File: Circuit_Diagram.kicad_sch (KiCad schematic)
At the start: 21 parts, among them IC1 HCPL-3120, Q2 Q_NMOS_GDS, U3 ACPL-C870, U4 ACS712xLCTR-30A

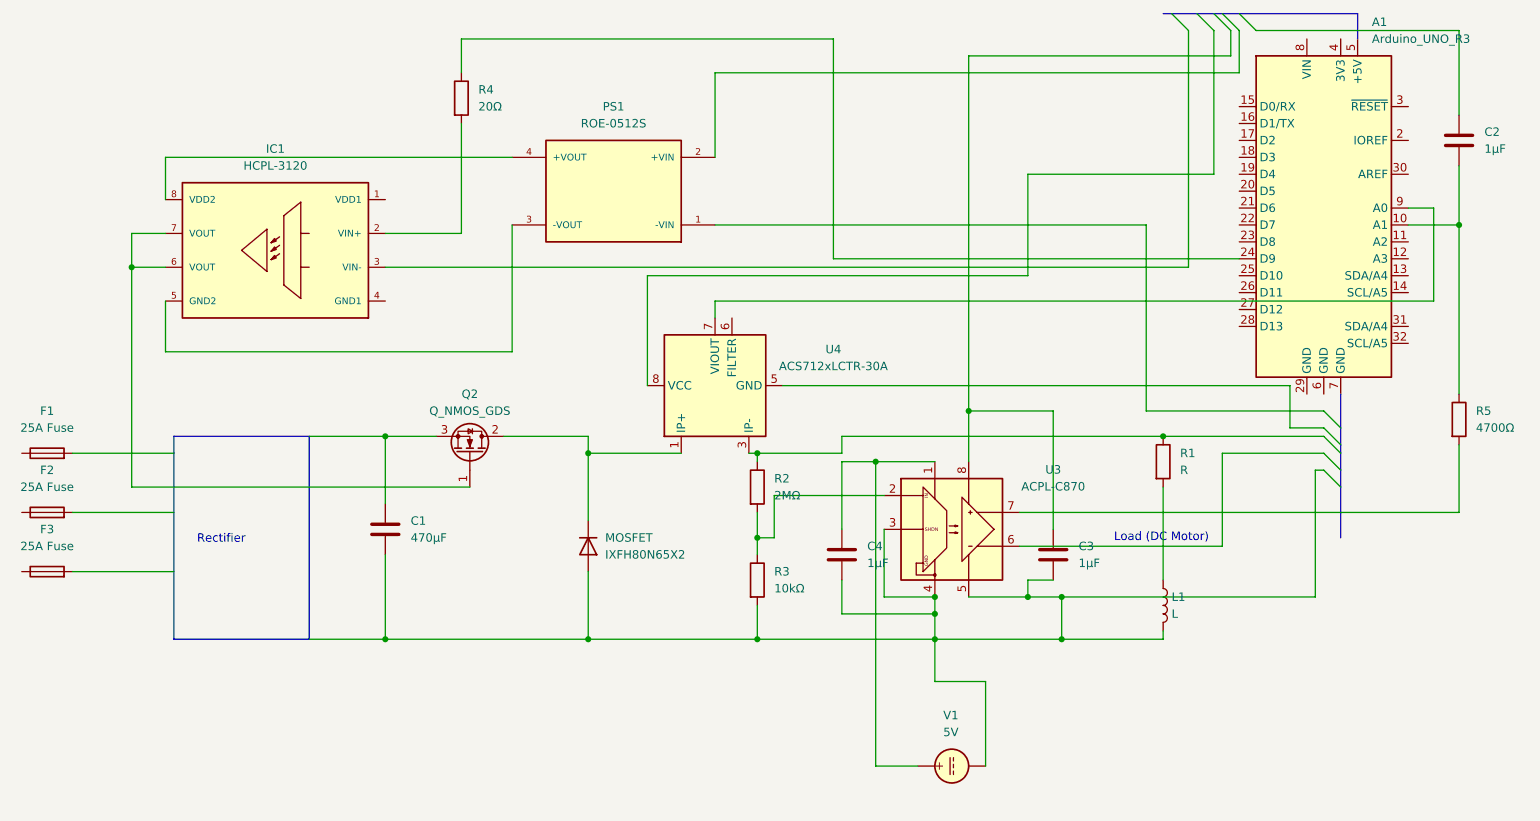
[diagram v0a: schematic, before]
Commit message: Updated wiring diagram
Added RC filter to voltage sensor output
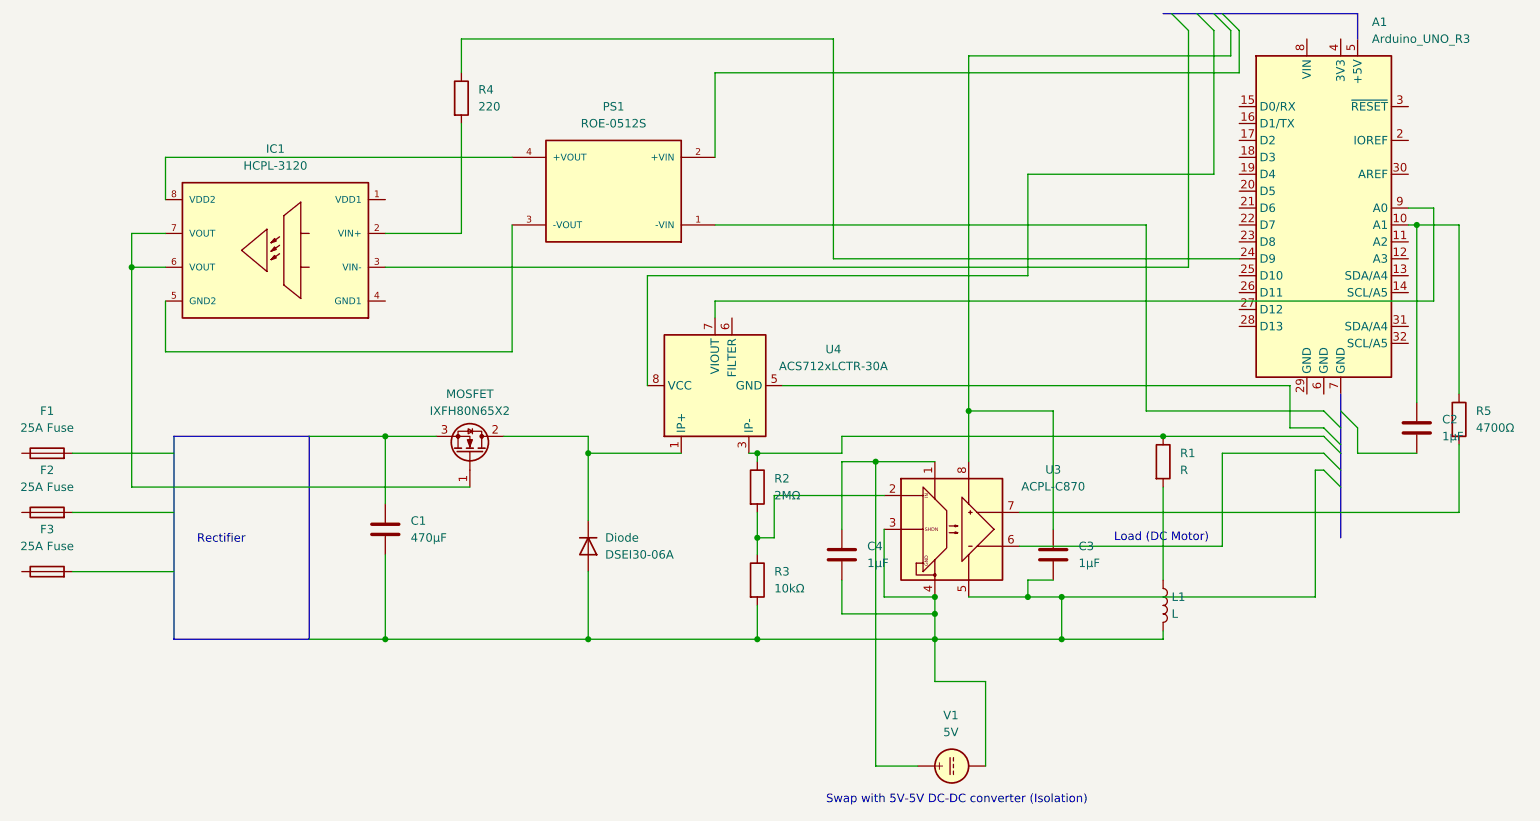
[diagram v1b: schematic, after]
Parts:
- Diode: renamed from MOSFET; value IXFH80N65X2 -> DSEI30-06A
- MOSFET: renamed from Q2; value Q_NMOS_GDS -> IXFH80N65X2
- R4: value 20Ω -> 220
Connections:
- net at A1.10 (A1), R5.1: now also C2.1; no longer C2.2
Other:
- note added: "Swap with 5V-5V DC-DC converter (Isolation)"
- moved on the sheet: C2
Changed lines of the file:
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@@
+		)
+	)
+	(text "Swap with 5V-5V DC-DC converter (Isolation)\n"
+		(exclude_from_sim no)
+		(at 158.242 132.08 0)
+		(effects
+			(font
+				(size 1.27 1.27)
+			)
 		)
 	)
@@
 	)
 	(junction
+		(at 227.33 45.72)
+		(diameter 0)
+		(color 0 0 0 0)
+	)
+	(junction
 		(at 72.39 77.47)
 		(diameter 0)
@@
 	)
 	(junction
-		(at 233.68 45.72)
-		(diameter 0)
-		(color 0 0 0 0)
-	)
-	(junction
 		(at 128.27 92.71)
 		(diameter 0)
@@
 	)
 	(bus_entry
-		(at 200.66 13.97)
-		(size 2.54 2.54)
-		(stroke
-			(width 0)
-			(type default)
-		)
-	)
-	(bus_entry
 		(at 213.36 76.2)
 		(size 2.54 2.54)
@@
 	)
 	(bus_entry
+		(at 215.9 73.66)
+		(size 2.54 2.54)
+		(stroke
+			(width 0)
+			(type default)
+		)
+	)
+	(bus_entry
 		(at 198.12 13.97)
 		(size 2.54 2.54)
@@
 		)
 	)
+	(wire
+		(pts
+			(xy 218.44 80.01) (xy 218.44 76.2)
+		)
+		(stroke
+			(width 0)
+			(type default)
+		)
+	)
 	(bus
 		(pts
-			(xy 198.12 13.97) (xy 200.66 13.97)
+			(xy 198.12 13.97) (xy 218.44 13.97)
 		)
 		(stroke
@@
 	(wire
 		(pts
+			(xy 227.33 80.01) (xy 218.44 80.01)
+		)
+		(stroke
+			(width 0)
+			(type default)
+		)
+	)
+	(wire
+		(pts
 			(xy 168.91 101.6) (xy 173.99 101.6)
 		)
@@
 	(wire
 		(pts
-			(xy 233.68 16.51) (xy 203.2 16.51)
-		)
-		(stroke
-			(width 0)
-			(type default)
-		)
-	)
-	(wire
-		(pts
 			(xy 167.64 88.9) (xy 233.68 88.9)
 		)
@@
 		)
 	)
+	(wire
+		(pts
+			(xy 72.39 52.07) (xy 193.04 52.07)
+		)
+		(stroke
+			(width 0)
+			(type default)
+		)
+	)
+	(wire
+		(pts
+			(xy 34.29 85.09) (xy 85.09 85.09)
+		)
+		(stroke
+			(width 0)
+			(type default)
+		)
+	)
+	(wire
+		(pts
+			(xy 154.94 81.28) (xy 146.05 81.28)
+		)
+		(stroke
+			(width 0)
+			(type default)
+		)
+	)
 	(bus
 		(pts
-			(xy 200.66 13.97) (xy 218.44 13.97)
-		)
-		(stroke
-			(width 0)
-			(type default)
-		)
-	)
-	(wire
-		(pts
-			(xy 72.39 52.07) (xy 193.04 52.07)
-		)
-		(stroke
-			(width 0)
-			(type default)
-		)
-	)
-	(wire
-		(pts
-			(xy 233.68 36.83) (xy 233.68 45.72)
-		)
-		(stroke
-			(width 0)
-			(type default)
-		)
-	)
-	(wire
-		(pts
-			(xy 34.29 85.09) (xy 85.09 85.09)
-		)
-		(stroke
-			(width 0)
-			(type default)
-		)
-	)
-	(wire
-		(pts
-			(xy 154.94 81.28) (xy 146.05 81.28)
+			(xy 215.9 73.66) (xy 215.9 76.2)
 		)
 		(stroke
@@
 	(wire
 		(pts
+			(xy 227.33 72.39) (xy 227.33 45.72)
+		)
+		(stroke
+			(width 0)
+			(type default)
+		)
+	)
+	(wire
+		(pts
 			(xy 102.87 97.79) (xy 102.87 107.95)
 		)
@@
 	(wire
 		(pts
+			(xy 227.33 45.72) (xy 233.68 45.72)
+		)
+		(stroke
+			(width 0)
+			(type default)
+		)
+	)
+	(wire
+		(pts
 			(xy 25.4 97.79) (xy 40.64 97.79)
 		)
@@
 	(wire
 		(pts
-			(xy 233.68 29.21) (xy 233.68 16.51)
-		)
-		(stroke
-			(width 0)
-			(type default)
-		)
-	)
-	(wire
-		(pts
 			(xy 198.12 80.01) (xy 198.12 93.98)
 		)
@@
 	(wire
 		(pts
-			(xy 226.06 45.72) (xy 233.68 45.72)
+			(xy 226.06 45.72) (xy 227.33 45.72)
 		)
 		(stroke
@@
 	(bus
 		(pts
-			(xy 215.9 71.12) (xy 215.9 76.2)
+			(xy 215.9 71.12) (xy 215.9 73.66)
 		)
 		(stroke
@@
 		(on_board yes)
 		(dnp no)
-		(property "Reference" "Q2"
+		(property "Reference" "MOSFET"
 			(at 85.09 71.12 90)
 			(effects
@@
 			)
 		)
-		(property "Value" "Q_NMOS_GDS"
+		(property "Value" "IXFH80N65X2"
 			(at 85.09 73.66 90)
 			(effects
@@
 			(project "Circuit_Diagram"
 				(path "/866ecc8a-ec11-4793-ac61-b439165b2991"
-					(reference "Q2")
+					(reference "MOSFET")
 					(unit 1)
 				)
@@
 			)
 		)
-		(property "Value" "20Ω"
+		(property "Value" "220"
 			(at 86.36 27.9399 0)
 			(effects
@@
 	(symbol
 		(lib_id "Device:C")
-		(at 233.68 33.02 0)
+		(at 227.33 76.2 0)
 		(unit 1)
 		(exclude_from_sim no)
@@
 		(fields_autoplaced yes)
 		(property "Reference" "C2"
-			(at 237.49 31.7499 0)
+			(at 231.14 74.9299 0)
 			(effects
 				(font
@@
 		)
 		(property "Value" "1μF"
-			(at 237.49 34.2899 0)
+			(at 231.14 77.4699 0)
 			(effects
 				(font
@@
 		)
 		(property "Footprint" ""
-			(at 234.6452 36.83 0)
+			(at 228.2952 80.01 0)
 			(effects
 				(font
@@
 		)
 		(property "Datasheet" "~"
-			(at 233.68 33.02 0)
+			(at 227.33 76.2 0)
 			(effects
 				(font
@@
 		)
 		(property "Description" "Unpolarized capacitor"
-			(at 233.68 33.02 0)
+			(at 227.33 76.2 0)
 			(effects
 				(font
@@
 		(dnp no)
 		(fields_autoplaced yes)
-		(property "Reference" "MOSFET"
+		(property "Reference" "Diode"
 			(at 105.41 92.7099 90)
 			(effects
@@
 			)
 		)
-		(property "Value" "IXFH80N65X2"
+		(property "Value" "DSEI30-06A"
 			(at 105.41 95.2499 90)
 			(effects
@@
 			(project ""
 				(path "/866ecc8a-ec11-4793-ac61-b439165b2991"
-					(reference "MOSFET")
+					(reference "Diode")
 					(unit 1)
 				)

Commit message: Updated Schematic
Replaced HCPL3120 DIP-8 with TLP250 DIP-8
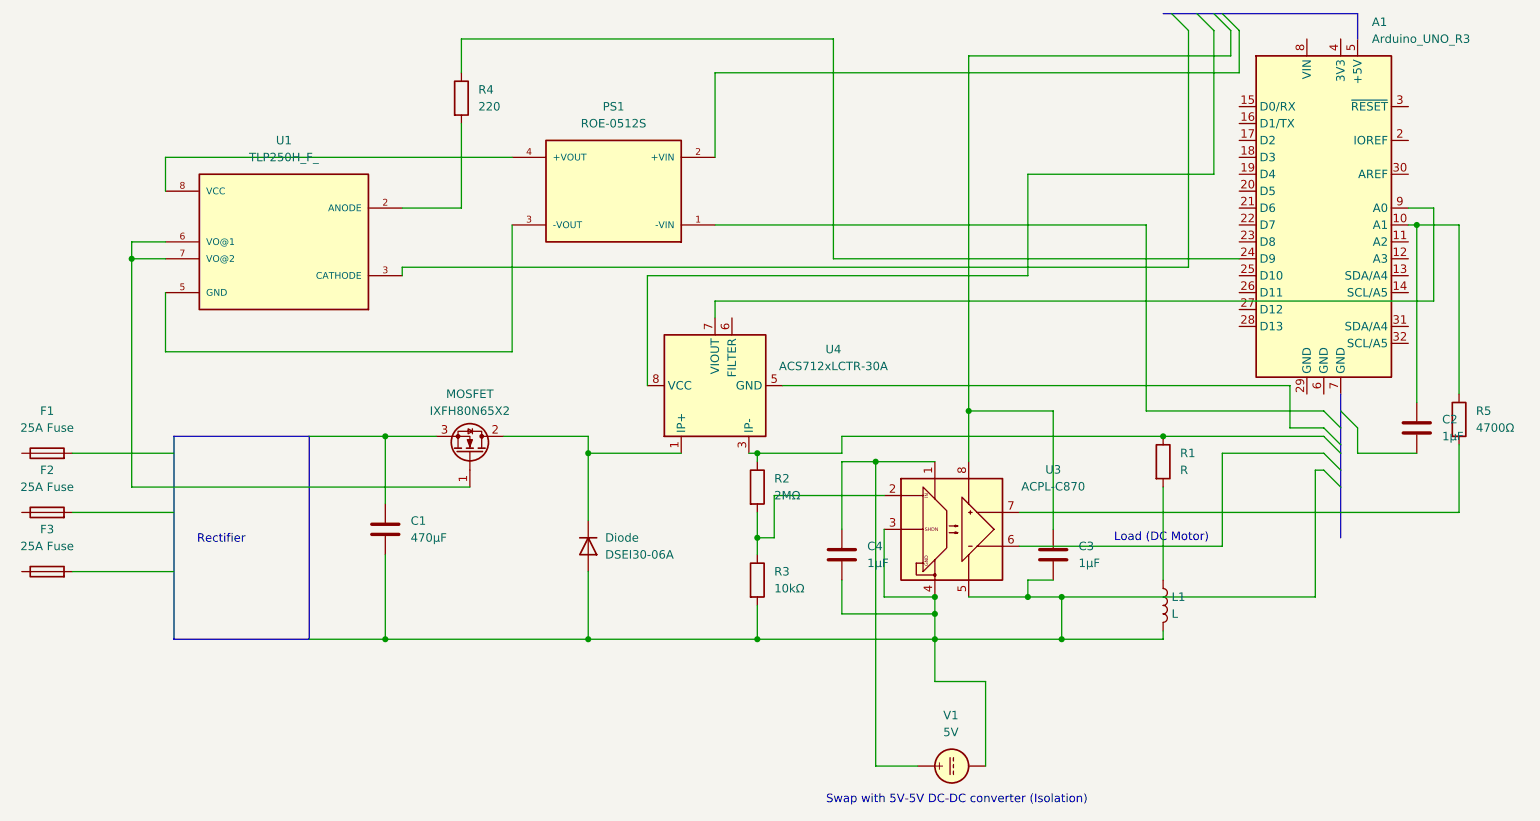
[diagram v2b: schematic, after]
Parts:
- removed IC1: HCPL-3120, symbol HCPL-3120:HCPL-3120
- added U1: TLP250H_F_, TLP250H_F_:DIP1016W50P254L966H380Q8P, symbol TLP250H_F_:TLP250H_F_
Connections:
- net at MOSFET.1 (G): now also U1.6 (VO@1), U1.7 (VO@2)
- net at R4.2: now also U1.2 (ANODE)
- net at PS1.3 (-VOUT): now also U1.5 (GND)
- net at PS1.4 (+VOUT): now also U1.8 (VCC)
